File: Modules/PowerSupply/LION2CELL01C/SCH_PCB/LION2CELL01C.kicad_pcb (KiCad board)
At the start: 2 copper layers, 80.8 x 60.5 mm, 96 parts, among them J1 JUMP_4X2, J10 JUMP_2x1, J11 JUMP_2x1, J12 JUMP_2x1, J13 JUMP_4X2, J14 JUMP_2x1, J2 JUMP_2x1, J3 JUMP_2x1, J4 JUMP_2x1, J5 JUMP_2x1, J6 JUMP_2x1, J7 JUMP_4X2, J8 CONN1_1, J9 CONN1_1, P1 _, P2 _, P3 _, P4 _, Q1 IRLML6244, Q2 MMBF170LT1G, Q3 MMBF170LT1G, Q4 BSS83P, SW1 SW_PUSH, U1 BQ29209, U2 BQ24103, U3 BQ34Z100, U4 SN74HC164D

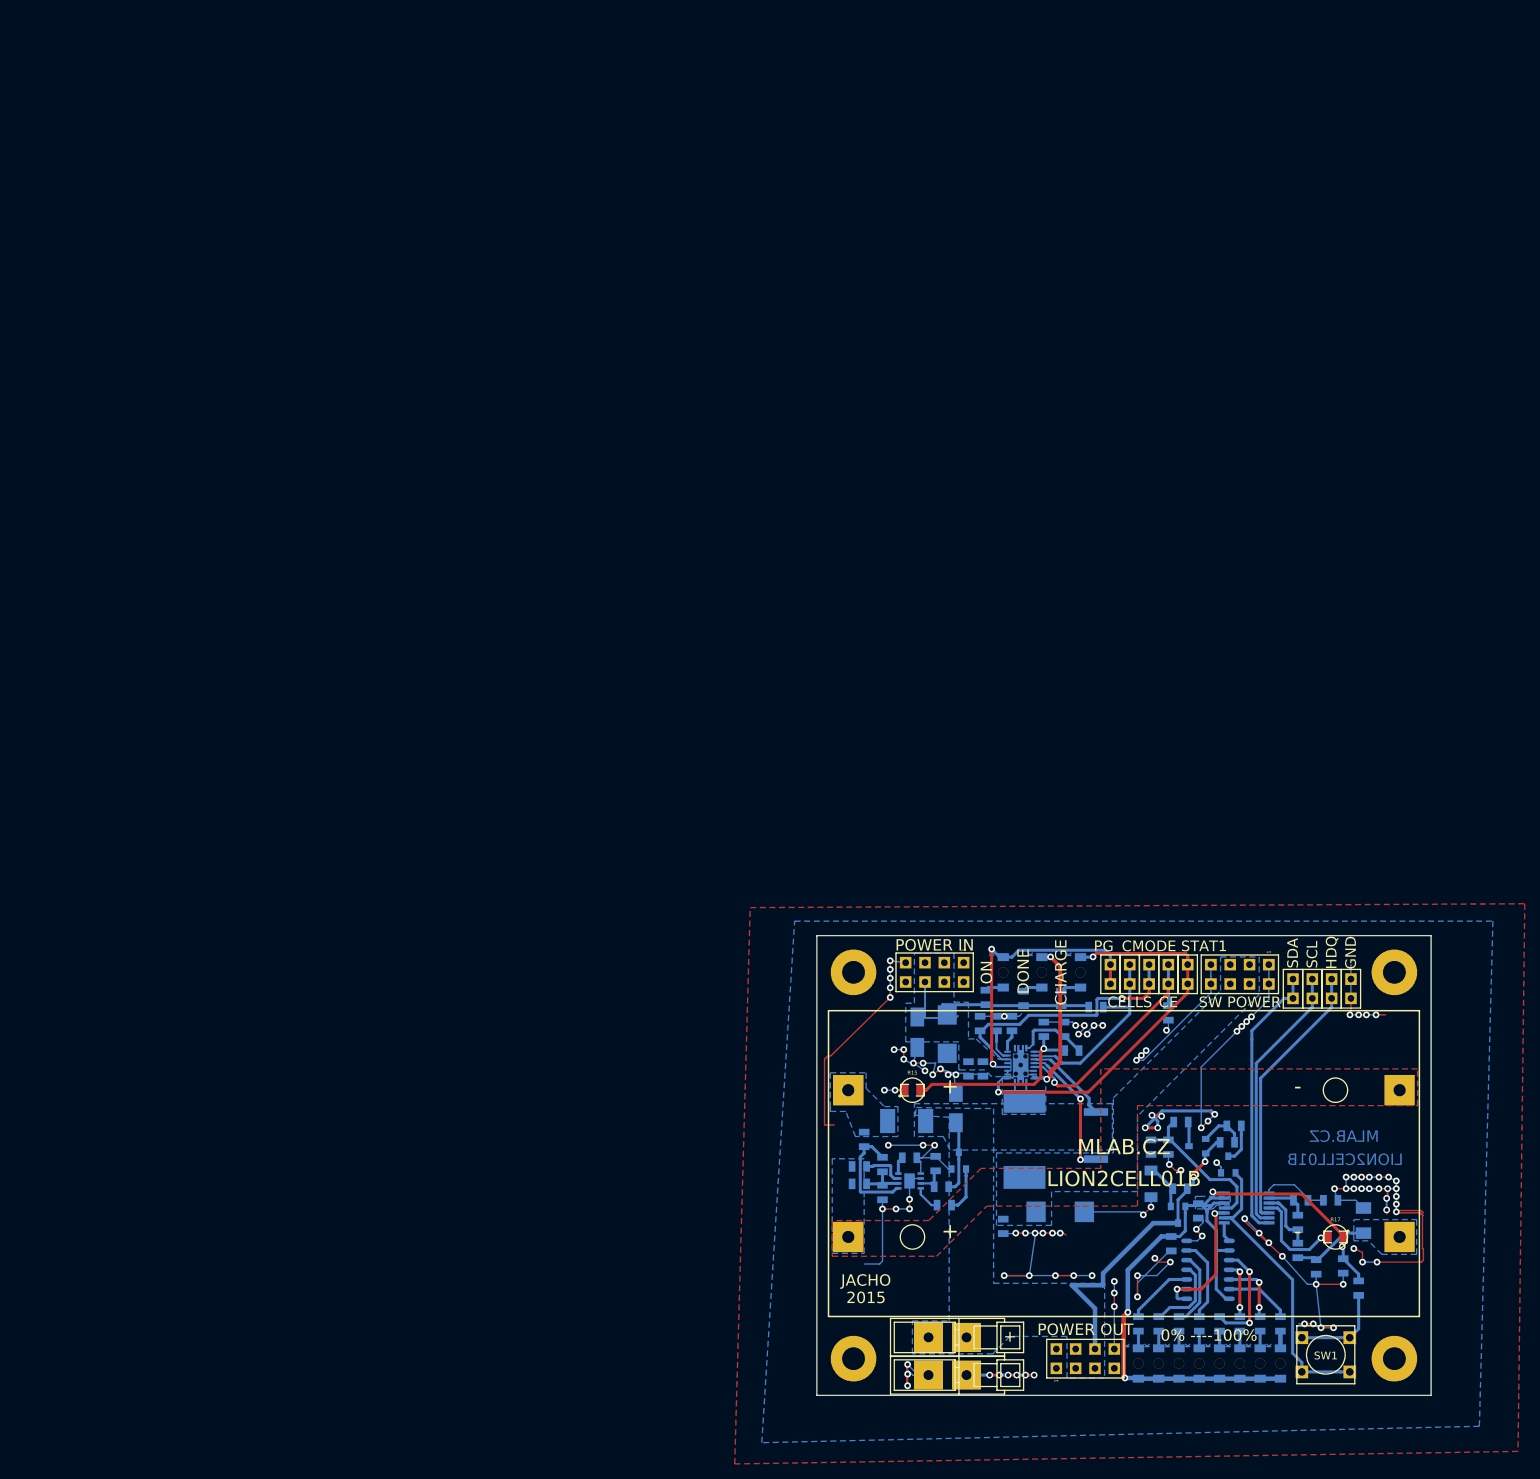
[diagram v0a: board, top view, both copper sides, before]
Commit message: 
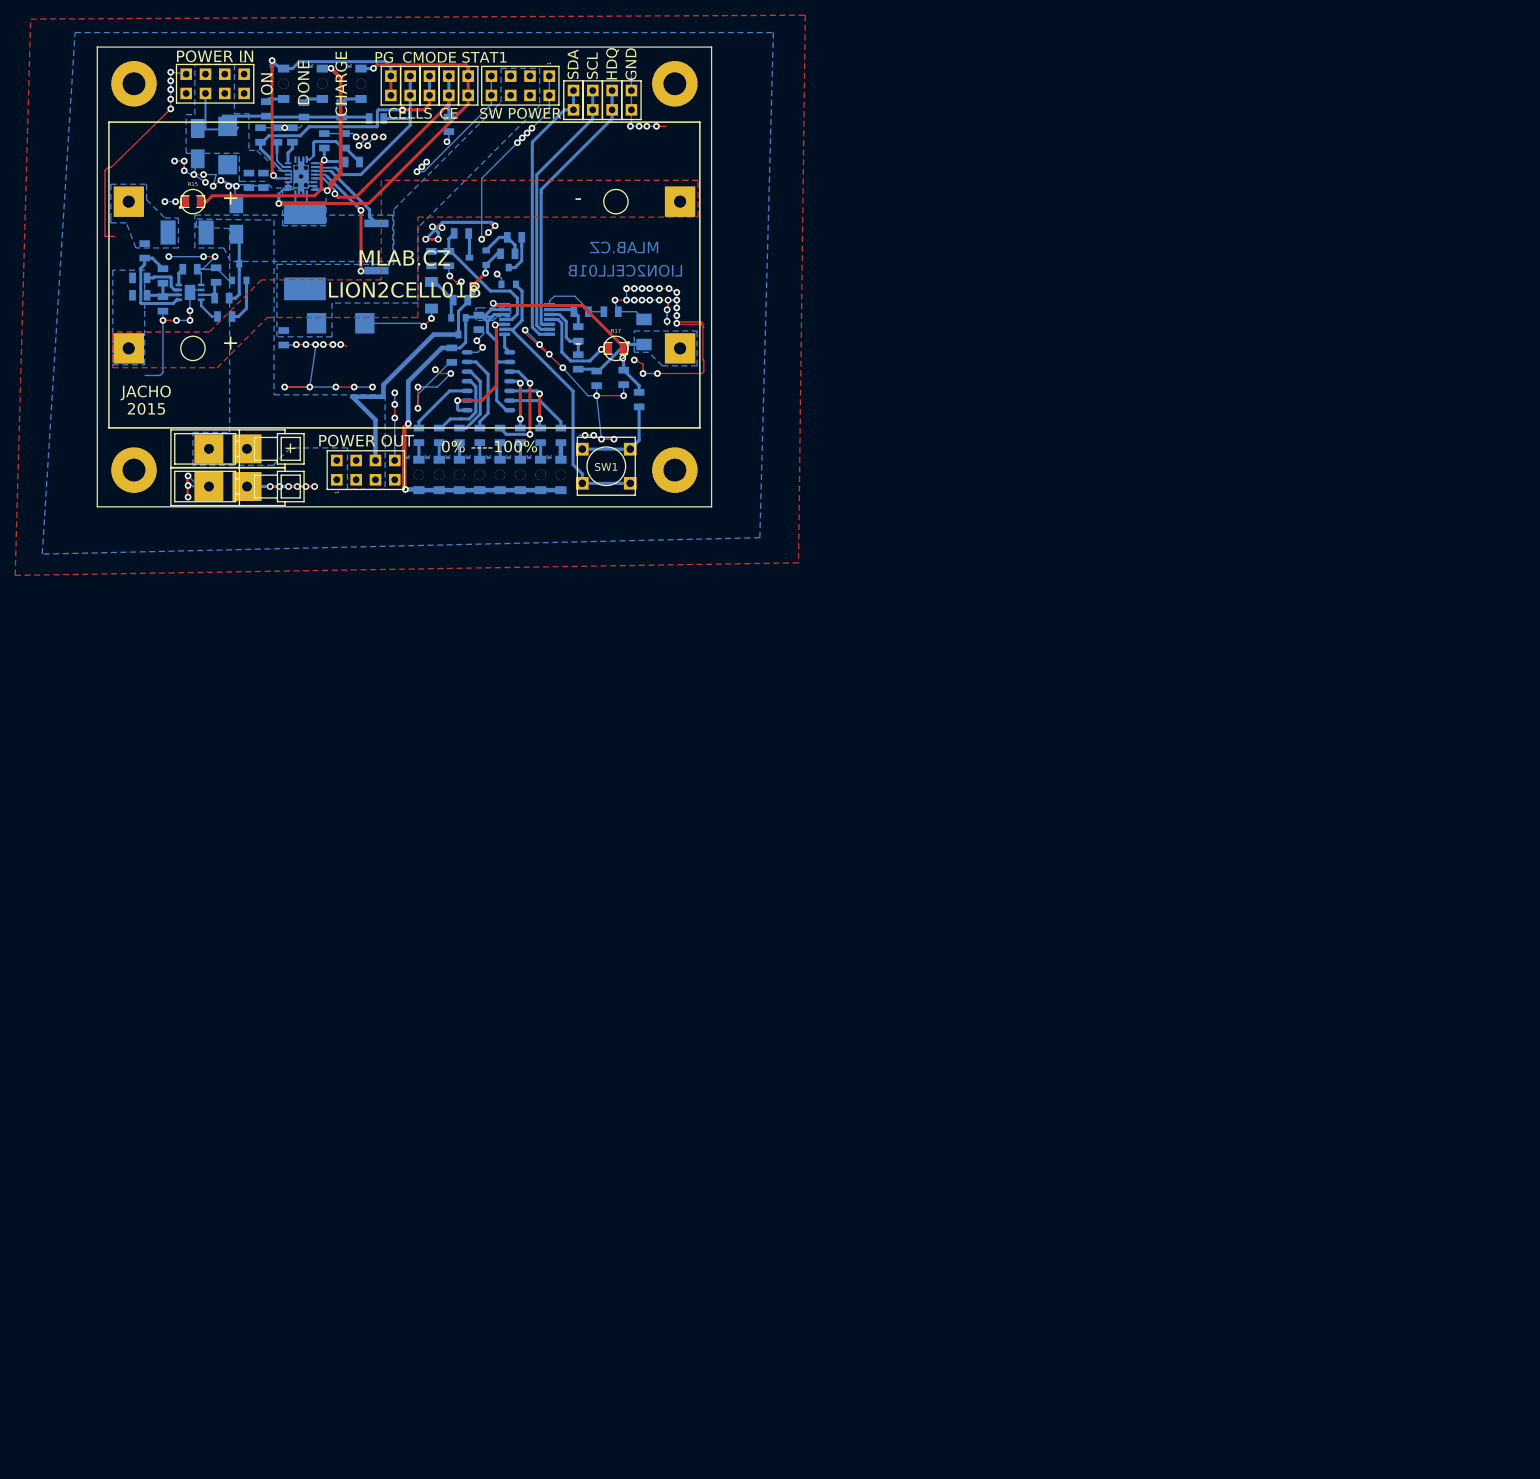
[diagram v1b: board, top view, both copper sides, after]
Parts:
- moved BT1 150.3 mm to (40.6, -30.7)
- moved C1 150.3 mm to (8.89, -26.9)
- moved C10 150.3 mm to (32.3, -24.4)
- moved C11 150.3 mm to (24.8, -22.5)
- moved C14 150.3 mm to (69.5, -17.3)
- moved C15 150.3 mm to (67.8, -25.9)
- moved C17 150.3 mm to (44.2, -32.9)
- moved C18 150.3 mm to (46.9, -20.2)
- moved C2 150.3 mm to (17.4, -47.8)
- moved C3 150.3 mm to (20.2, -43.2)
- moved C4 150.3 mm to (8.89, -30.6)
- moved C6 150.3 mm to (21.7, -49.1)
- moved C7 150.3 mm to (22.1, -43.2)
- moved C8 150.3 mm to (15.9, -30.7)
- moved C9 150.3 mm to (32.8, -48.4)
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
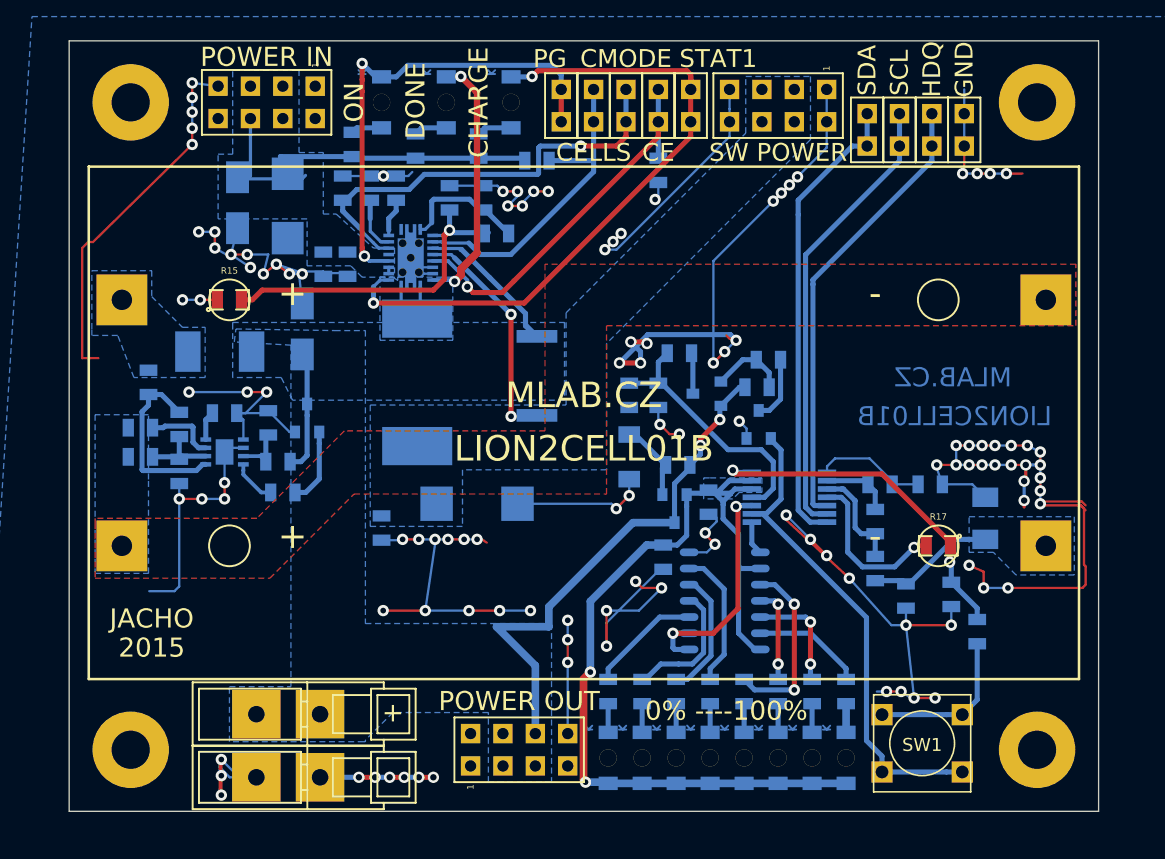
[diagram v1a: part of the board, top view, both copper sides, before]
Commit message: 
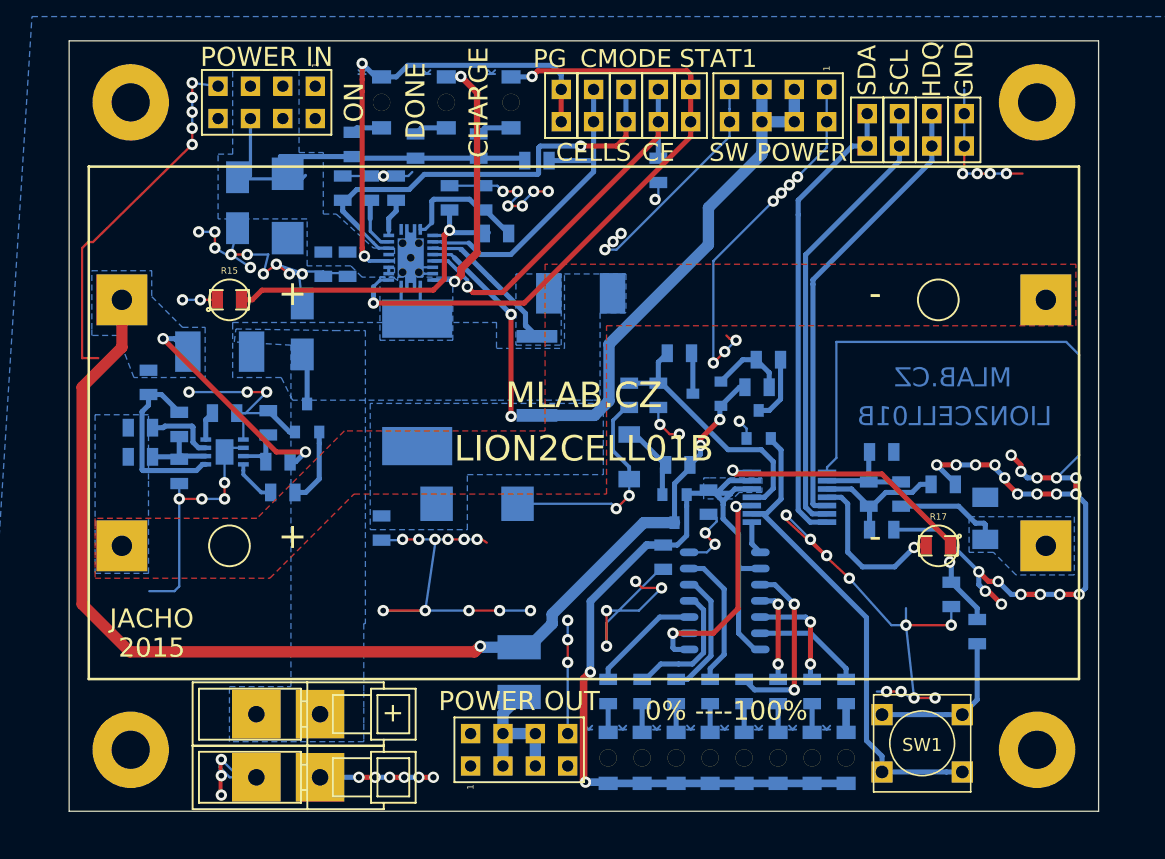
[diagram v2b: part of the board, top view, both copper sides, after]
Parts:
- added F2: 1,1A, Mlab_F:1812, B.Cu at (35.6, -11.2)
- added F3: 2A, Mlab_F:2410, B.Cu at (40.4, -40.9)
- C5: value 100nF -> 330nF
- F1: value FUSE -> 5A
- R1: value 1K -> 160R
- R2: value 1K -> 260R
- R24: value divider.1% 25ppm -> 140k .1% 25ppm
- R3: value 240R -> 100R
- moved C16 11.5 mm to (64.0, -28.4), turned to 0 degrees
- moved R18 6.19 mm to (65.5, -25.1)
- moved C15 5.21 mm to (64.0, -22.4), turned to 0 degrees
- moved R19 4.95 mm to (68.8, -25.9)
- moved C13 2.22 mm to (63.0, -25.1), turned to 270 degrees
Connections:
- C15 pad 1: GND -> Net-(C13-Pad2)
- C16 pad 1: /BATTERY- -> Net-(C13-Pad1)
- J7 pad 3: /BATTERY+ -> Net-(F2-Pad1)
- J7 pad 4: /BATTERY+ -> Net-(F2-Pad1)
- J7 pad 5: /BATTERY+ -> Net-(F2-Pad1)
- J7 pad 6: /BATTERY+ -> Net-(F2-Pad1)
- Q2 pad D: /BATTERY+ -> /BAT+
- Q4 pad S: /BATTERY+ -> /BAT+
- R16 pad 1: /BATTERY+ -> Net-(F3-Pad1)
- R21 pad 2: /BATTERY+ -> /BAT+
- R26 pad 1: /BATTERY+ -> /BAT+
- R9 pad 2: /BATTERY+ -> /BAT+
- U2 pad 11: Net-(C9-Pad1) -> (no net)
- U2 pad 14: /BATTERY+ -> Net-(F3-Pad1)
- U3 pad 10: Net-(C13-Pad1) -> Net-(C13-Pad2)
- U3 pad 4: Net-(C17-Pad1) -> (no net)
- U3 pad 9: Net-(C13-Pad2) -> Net-(C13-Pad1)
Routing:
- net /BAT+: track 0.00 -> 110.0 mm, vias 0 -> 5
- net /BATTERY+: track 63.9 -> 4.04 mm, vias 2 -> 0
- net Net-(C10-Pad1): track 16.1 -> 56.7 mm
- net GND: track 395.9 -> 414.6 mm, vias 117 -> 112
- net Net-(F3-Pad1): track 0.00 -> 13.0 mm
- net Net-(F2-Pad1): track 0.00 -> 11.0 mm
- net Net-(C13-Pad2): track 5.53 -> 11.3 mm
- net /BATTERY-: track 10.2 -> 8.36 mm
- added copper zone on B.Cu, net Net-(F3-Pad1)
